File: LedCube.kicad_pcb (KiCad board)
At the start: 4 copper layers, 87.7 x 80.2 mm, 334 parts, among them CN1 B2B-XH-A (LF)(SN), CN2 B2B-XH-A (LF)(SN), J1 B10B-PHDSS-B_LF__SN_, J10 B10B-PHDSS-B_LF__SN_, J11 B10B-PHDSS-B_LF__SN_, J2 B10B-PHDSS-B_LF__SN_, J3 B10B-PHDSS-B_LF__SN_, J4 B10B-PHDSS-B_LF__SN_, J5 B10B-PHDSS-B_LF__SN_, J6 B10B-PHDSS-B_LF__SN_, J7 B10B-PHDSS-B_LF__SN_, J8 B10B-PHDSS-B_LF__SN_, J9 B10B-PHDSS-B_LF__SN_, Q1 AO3400A, Q10 AO3400A, Q11 JSM7409B, Q13 JSM7409B, Q2 AO3400A, Q3 AO3400A, Q4 AO3400A, Q5 AO3400A, Q6 AO3400A, Q7 AO3400A, Q8 AO3400A, Q9 AO3400A, SW2 TS-1088-AR02016, U1 STM32H743VGTx, U10 SN74LVC373ARGYR, U11 SN74LVC373ARGYR, U12 SN74LVC373ARGYR, U13 SN74LVC373ARGYR, U14 SN74LVC373ARGYR, U15 SN74LVC373ARGYR, U16 SN74LVC373ARGYR, U17 SN74LVC373ARGYR, U18 SN74LVC373ARGYR, U19 SN74LVC373ARGYR, U2 M95M04-DRMN6TP, U20 STUSB4500QTR, U21 ASM330LHBG1TR, U22 IIS2MDCTR, U23 TMP117xxDRV, U24 CC1101RGPR, U25 CC1101RGPR, U3 B3B-XH-A(LF)(SN), U4 B4B-XH-A(LF)(SN), U5 HC-PHD2.0-2X3A, U6 TPS56637RPAR, U7 SN74LVC373ARGYR, U8 SN74LVC373ARGYR, U9 SN74LVC373ARGYR, X1 Q13FC1350000400, Y1 MDH 2.D.1.480008813, Y3 Crystal_GND24, Y4 Crystal_GND24

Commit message: Update PCB layout
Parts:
- added REF**: MountingHole_2mm, MountingHole:MountingHole_2mm, F.Cu at (117.9, 38.6)
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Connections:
- D14 pad 4: unconnected-(D14-K3-Pad4) -> Net-(D14-K3)
- D14 pad 5: unconnected-(D14-K4-Pad5) -> Net-(D14-K4)
- D14 pad 8: Net-(D14-K7) -> unconnected-(D14-K7-Pad8)
- D14 pad 9: Net-(D14-K8) -> unconnected-(D14-K8-Pad9)
- D15 pad 4: unconnected-(D15-K3-Pad4) -> Net-(D15-K3)
- D15 pad 5: unconnected-(D15-K4-Pad5) -> Net-(D15-K4)
- D15 pad 6: Net-(D15-K5) -> unconnected-(D15-K5-Pad6)
- D15 pad 7: Net-(D15-K6) -> unconnected-(D15-K6-Pad7)
- D18 pad 4: Net-(D18-K3) -> unconnected-(D18-K3-Pad4)
- D18 pad 8: unconnected-(D18-K7-Pad8) -> Net-(D18-K7)
- D19 pad 2: Net-(D19-K2) -> unconnected-(D19-K2-Pad2)
- D19 pad 7: unconnected-(D19-K6-Pad7) -> Net-(D19-K6)
- D8 pad 2: Net-(D8-K2) -> unconnected-(D8-K2-Pad2)
- D8 pad 9: Net-(D8-K8) -> Net-(D5-K1)
- J1 pad 1: Net-(J1-Pad1) -> Net-(D5-K1)
- J1 pad 10: Net-(J1-Pad10) -> Net-(D5-K8)
- J1 pad 2: Net-(J1-Pad2) -> Net-(D8-K1)
- J1 pad 3: Net-(J1-Pad3) -> Net-(D5-K5)
- J1 pad 4: Net-(J1-Pad4) -> Net-(D5-K4)
- J1 pad 5: Net-(J1-Pad5) -> Net-(D5-K6)
- J1 pad 6: Net-(J1-Pad6) -> Net-(D5-K3)
- J1 pad 7: Net-(J1-Pad7) -> Net-(D5-K2)
- J1 pad 8: Net-(J1-Pad8) -> Net-(D5-K7)
- J1 pad 9: Net-(J1-Pad9) -> Net-(D5-K1)
- J10 pad 1: Net-(J10-Pad1) -> Net-(D16-K7)
- J10 pad 10: Net-(J10-Pad10) -> Net-(D17-K4)
- J10 pad 2: Net-(J10-Pad2) -> Net-(D17-K8)
- J10 pad 3: Net-(J10-Pad3) -> Net-(D16-K8)
- J10 pad 4: Net-(J10-Pad4) -> Net-(D17-K7)
- J10 pad 5: Net-(J10-Pad5) -> Net-(D17-K1)
- J10 pad 6: Net-(J10-Pad6) -> Net-(D17-K6)
- J10 pad 7: Net-(J10-Pad7) -> Net-(D17-K2)
- J10 pad 8: Net-(J10-Pad8) -> Net-(D17-K5)
- J10 pad 9: Net-(J10-Pad9) -> Net-(D17-K3)
- J11 pad 3: Net-(D19-K2) -> Net-(D19-K3)
- J11 pad 4: Net-(D19-K3) -> Net-(D19-K6)
- J11 pad 8: Net-(D18-K3) -> Net-(D18-K7)
- J2 pad 1: Net-(J2-Pad1) -> Net-(D6-K1)
- J2 pad 10: Net-(J2-Pad10) -> Net-(D6-K6)
- J2 pad 2: Net-(J2-Pad2) -> Net-(D9-K2)
- J2 pad 3: Net-(J2-Pad3) -> Net-(D6-K2)
- J2 pad 4: Net-(J2-Pad4) -> Net-(D9-K1)
- J2 pad 5: Net-(J2-Pad5) -> Net-(D6-K3)
- J2 pad 6: Net-(J2-Pad6) -> Net-(D6-K8)
- J2 pad 7: Net-(J2-Pad7) -> Net-(D6-K4)
- J2 pad 8: Net-(J2-Pad8) -> Net-(D6-K7)
- J2 pad 9: Net-(J2-Pad9) -> Net-(D6-K5)
- J3 pad 1: Net-(J3-Pad1) -> Net-(D7-K1)
- J3 pad 10: Net-(J3-Pad10) -> Net-(D7-K6)
- J3 pad 2: Net-(J3-Pad2) -> Net-(D10-K2)
- J3 pad 3: Net-(J3-Pad3) -> Net-(D7-K2)
- J3 pad 4: Net-(J3-Pad4) -> Net-(D10-K1)
- J3 pad 5: Net-(J3-Pad5) -> Net-(D7-K3)
- J3 pad 6: Net-(J3-Pad6) -> Net-(D7-K8)
- J3 pad 7: Net-(J3-Pad7) -> Net-(D7-K4)
- J3 pad 8: Net-(J3-Pad8) -> Net-(D7-K7)
- J3 pad 9: Net-(J3-Pad9) -> Net-(D7-K5)
- J4 pad 1: Net-(J4-Pad1) -> Net-(D8-K3)
- J4 pad 2: Net-(J4-Pad2) -> Net-(D11-K4)
- J4 pad 3: Net-(J4-Pad3) -> Net-(D8-K4)
- J4 pad 4: Net-(J4-Pad4) -> Net-(D11-K3)
- J4 pad 5: Net-(J4-Pad5) -> Net-(D8-K5)
- J4 pad 6: Net-(J4-Pad6) -> Net-(D11-K2)
- J4 pad 7: Net-(J4-Pad7) -> Net-(D8-K6)
- J4 pad 8: Net-(J4-Pad8) -> Net-(D11-K1)
- J4 pad 9: Net-(J4-Pad9) -> Net-(D8-K7)
- J5 pad 1: Net-(J5-Pad1) -> Net-(D9-K3)
- J5 pad 10: Net-(J5-Pad10) -> Net-(D9-K8)
- J5 pad 2: Net-(J5-Pad2) -> Net-(D12-K4)
- J5 pad 3: Net-(J5-Pad3) -> Net-(D9-K4)
- J5 pad 4: Net-(J5-Pad4) -> Net-(D12-K3)
- J5 pad 5: Net-(J5-Pad5) -> Net-(D9-K5)
- J5 pad 6: Net-(J5-Pad6) -> Net-(D12-K2)
- J5 pad 7: Net-(J5-Pad7) -> Net-(D9-K6)
- J5 pad 8: Net-(J5-Pad8) -> Net-(D12-K1)
- J5 pad 9: Net-(J5-Pad9) -> Net-(D9-K7)
- J6 pad 1: Net-(J6-Pad1) -> Net-(D10-K3)
- J6 pad 10: Net-(J6-Pad10) -> Net-(D10-K8)
- J6 pad 2: Net-(J6-Pad2) -> Net-(D13-K4)
- J6 pad 3: Net-(J6-Pad3) -> Net-(D10-K4)
- J6 pad 4: Net-(J6-Pad4) -> Net-(D13-K3)
- J6 pad 5: Net-(J6-Pad5) -> Net-(D10-K5)
- J6 pad 6: Net-(J6-Pad6) -> Net-(D13-K2)
- J6 pad 7: Net-(J6-Pad7) -> Net-(D10-K6)
- J6 pad 8: Net-(J6-Pad8) -> Net-(D13-K1)
- J6 pad 9: Net-(J6-Pad9) -> Net-(D10-K7)
- J7 pad 1: Net-(J7-Pad1) -> Net-(D11-K5)
- J7 pad 10: Net-(J7-Pad10) -> Net-(D14-K2)
- J7 pad 2: Net-(J7-Pad2) -> Net-(D14-K6)
- J7 pad 3: Net-(J7-Pad3) -> Net-(D11-K6)
- J7 pad 4: Net-(J7-Pad4) -> Net-(D14-K5)
- J7 pad 5: Net-(J7-Pad5) -> Net-(D11-K7)
- J7 pad 6: Net-(J7-Pad6) -> Net-(D14-K4)
- J7 pad 7: Net-(J7-Pad7) -> Net-(D11-K8)
- J7 pad 8: Net-(J7-Pad8) -> Net-(D14-K3)
- J7 pad 9: Net-(J7-Pad9) -> Net-(D14-K1)
- J8 pad 1: Net-(J8-Pad1) -> Net-(D12-K5)
- J8 pad 10: Net-(J8-Pad10) -> Net-(D15-K2)
- J8 pad 2: Net-(J8-Pad2) -> Net-(D15-K8)
- J8 pad 3: Net-(J8-Pad3) -> Net-(D12-K6)
- J8 pad 4: Net-(J8-Pad4) -> Net-(D15-K7)
- J8 pad 5: Net-(J8-Pad5) -> Net-(D12-K7)
- J8 pad 6: Net-(J8-Pad6) -> Net-(D15-K4)
- J8 pad 7: Net-(J8-Pad7) -> Net-(D12-K8)
- J8 pad 8: Net-(J8-Pad8) -> unconnected-(J8-Pad8)
- J8 pad 9: Net-(J8-Pad9) -> Net-(D15-K1)
- J9 pad 1: Net-(J9-Pad1) -> Net-(D13-K5)
- J9 pad 10: Net-(J9-Pad10) -> Net-(D16-K2)
- J9 pad 2: Net-(J9-Pad2) -> Net-(D16-K6)
- J9 pad 3: Net-(J9-Pad3) -> Net-(D13-K6)
- J9 pad 4: Net-(J9-Pad4) -> Net-(D16-K5)
- J9 pad 5: Net-(J9-Pad5) -> Net-(D13-K7)
- J9 pad 6: Net-(J9-Pad6) -> Net-(D16-K4)
- J9 pad 7: Net-(J9-Pad7) -> Net-(D13-K8)
- J9 pad 8: Net-(J9-Pad8) -> Net-(D16-K3)
- J9 pad 9: Net-(J9-Pad9) -> Net-(D16-K1)
- Q11 pad 6: /USB-PD/V_SINK -> (no net)
- Q11 pad 7: /USB-PD/V_SINK -> (no net)
- Q11 pad 8: /USB-PD/V_SINK -> (no net)
- Q13 pad 6: Net-(D21-K) -> (no net)
- Q13 pad 7: Net-(D21-K) -> (no net)
- Q13 pad 8: Net-(D21-K) -> (no net)
- Q2 pad 3: Net-(D18-K3) -> Net-(D18-K7)
- Q4 pad 3: Net-(D19-K3) -> Net-(D19-K6)
- Q7 pad 3: Net-(D19-K2) -> Net-(D19-K3)
- R100 pad 1: Net-(J9-Pad10) -> Net-(D16-K2)
- R100 pad 2: Net-(D16-K2) -> Net-(U18-2Q)
- R101 pad 1: Net-(J9-Pad8) -> Net-(D16-K3)
- R101 pad 2: Net-(D16-K8) -> Net-(U18-3Q)
- R102 pad 1: Net-(J9-Pad6) -> Net-(D16-K4)
- R102 pad 2: Net-(D16-K7) -> Net-(U18-4Q)
- R103 pad 1: Net-(J9-Pad4) -> unconnected-(R103-Pad1)
- R103 pad 2: Net-(D16-K6) -> Net-(D16-K5)
- R104 pad 1: Net-(J9-Pad2) -> unconnected-(R104-Pad1)
- R104 pad 2: Net-(D16-K5) -> Net-(D16-K6)
- R105 pad 1: Net-(D17-K8) -> Net-(D17-K3)
- R105 pad 2: Net-(J10-Pad9) -> Net-(U19-3Q)
- R106 pad 2: Net-(J10-Pad7) -> Net-(U19-2Q)
- R107 pad 2: Net-(J10-Pad5) -> Net-(U19-1Q)
- R108 pad 1: Net-(D16-K4) -> unconnected-(R108-Pad1)
- R108 pad 2: Net-(J10-Pad3) -> Net-(D16-K8)
- R109 pad 1: Net-(D16-K3) -> unconnected-(R109-Pad1)
- R109 pad 2: Net-(J10-Pad1) -> Net-(D16-K7)
- R110 pad 1: Net-(J10-Pad10) -> Net-(D17-K4)
- R110 pad 2: Net-(D17-K7) -> Net-(U19-4Q)
- R111 pad 1: Net-(J10-Pad8) -> unconnected-(R111-Pad1)
- R111 pad 2: Net-(D17-K6) -> Net-(D17-K5)
- R112 pad 1: Net-(J10-Pad6) -> unconnected-(R112-Pad1)
- R112 pad 2: Net-(D17-K5) -> Net-(D17-K6)
- R113 pad 1: Net-(J10-Pad4) -> unconnected-(R113-Pad1)
- R113 pad 2: Net-(D17-K3) -> Net-(D17-K7)
- R114 pad 1: Net-(J10-Pad2) -> unconnected-(R114-Pad1)
- R114 pad 2: Net-(D17-K4) -> Net-(D17-K8)
- R15 pad 1: Net-(D5-K6) -> Net-(D5-K5)
- R15 pad 2: Net-(J1-Pad9) -> unconnected-(R15-Pad2)
- R16 pad 1: Net-(D5-K7) -> unconnected-(R16-Pad1)
- R16 pad 2: Net-(J1-Pad7) -> Net-(D5-K4)
- R17 pad 1: Net-(D5-K8) -> unconnected-(R17-Pad1)
- R17 pad 2: Net-(J1-Pad5) -> Net-(D5-K3)
- R18 pad 1: Net-(D5-K2) -> Net-(U7-3Q)
- R18 pad 2: Net-(J1-Pad3) -> Net-(D5-K2)
- R19 pad 2: Net-(J1-Pad1) -> Net-(U7-1Q)
- R20 pad 1: Net-(D8-K3) -> unconnected-(R20-Pad1)
- R20 pad 2: Net-(J4-Pad9) -> Net-(D8-K7)
- R21 pad 1: Net-(D8-K5) -> unconnected-(R21-Pad1)
- R21 pad 2: Net-(J4-Pad7) -> Net-(D8-K6)
- R22 pad 1: Net-(D8-K6) -> unconnected-(R22-Pad1)
- R22 pad 2: Net-(J4-Pad5) -> Net-(D8-K5)
- R23 pad 1: Net-(D8-K7) -> Net-(D8-K4)
- R23 pad 2: Net-(J4-Pad3) -> Net-(U10-4Q)
- R24 pad 1: Net-(D8-K8) -> Net-(D8-K3)
- R24 pad 2: Net-(J4-Pad1) -> Net-(U10-3Q)
- R25 pad 1: Net-(J4-Pad10) -> unconnected-(R25-Pad1)
- R25 pad 2: Net-(D8-K4) -> Net-(J4-Pad10)
- R26 pad 1: Net-(J4-Pad8) -> Net-(D11-K1)
- R26 pad 2: Net-(D11-K1) -> Net-(U13-1Q)
- R27 pad 1: Net-(J4-Pad6) -> Net-(D11-K2)
- R27 pad 2: Net-(D11-K2) -> Net-(U13-2Q)
- R28 pad 1: Net-(J4-Pad4) -> Net-(D11-K3)
- R28 pad 2: Net-(D11-K8) -> Net-(U13-3Q)
- R29 pad 1: Net-(J4-Pad2) -> Net-(D11-K4)
- R29 pad 2: Net-(D11-K7) -> Net-(U13-4Q)
- R30 pad 1: Net-(J1-Pad10) -> Net-(D5-K6)
- R30 pad 2: Net-(D5-K5) -> unconnected-(R30-Pad2)
- R31 pad 1: Net-(J1-Pad8) -> Net-(D5-K6)
- R31 pad 2: Net-(D5-K3) -> Net-(U7-4Q)
- R32 pad 1: Net-(J1-Pad6) -> Net-(D5-K8)
- R32 pad 2: Net-(D5-K4) -> Net-(U7-2Q)
- R33 pad 1: Net-(J1-Pad4) -> Net-(D5-K4)
- R33 pad 2: Net-(D8-K1) -> Net-(U10-1Q)
- R34 pad 1: Net-(J1-Pad2) -> Net-(D8-K1)
- R34 pad 2: Net-(D8-K2) -> Net-(U10-2Q)
- R35 pad 2: Net-(J7-Pad9) -> Net-(U16-1Q)
- R36 pad 1: Net-(D11-K4) -> unconnected-(R36-Pad1)
- R36 pad 2: Net-(J7-Pad7) -> Net-(D11-K8)
- R37 pad 1: Net-(D11-K3) -> unconnected-(R37-Pad1)
- R37 pad 2: Net-(J7-Pad5) -> Net-(D11-K7)
- R38 pad 1: Net-(D11-K5) -> unconnected-(R38-Pad1)
- R38 pad 2: Net-(J7-Pad3) -> Net-(D11-K6)
- R39 pad 1: Net-(D11-K6) -> unconnected-(R39-Pad1)
- R39 pad 2: Net-(J7-Pad1) -> Net-(D11-K5)
- R40 pad 1: Net-(J7-Pad10) -> Net-(D14-K2)
- R40 pad 2: Net-(D14-K2) -> Net-(U16-2Q)
- R41 pad 1: Net-(J7-Pad8) -> Net-(D14-K3)
- R41 pad 2: Net-(D14-K8) -> Net-(U16-3Q)
- R42 pad 1: Net-(J7-Pad6) -> Net-(D14-K4)
- R42 pad 2: Net-(D14-K7) -> Net-(U16-4Q)
- R43 pad 1: Net-(J7-Pad4) -> unconnected-(R43-Pad1)
- R43 pad 2: Net-(D14-K6) -> Net-(D14-K5)
- R44 pad 1: Net-(J7-Pad2) -> unconnected-(R44-Pad1)
- R44 pad 2: Net-(D14-K5) -> Net-(D14-K6)
- R45 pad 1: Net-(D6-K6) -> unconnected-(R45-Pad1)
- R45 pad 2: Net-(J2-Pad9) -> Net-(D6-K5)
- R46 pad 1: Net-(D6-K7) -> Net-(D6-K4)
- R46 pad 2: Net-(J2-Pad7) -> Net-(U8-4Q)
- R47 pad 1: Net-(D6-K8) -> Net-(D6-K3)
- R47 pad 2: Net-(J2-Pad5) -> Net-(U8-3Q)
- R48 pad 2: Net-(J2-Pad3) -> Net-(U8-2Q)
- R49 pad 2: Net-(J2-Pad1) -> Net-(U8-1Q)
- R50 pad 1: Net-(J2-Pad10) -> unconnected-(R50-Pad1)
- R50 pad 2: Net-(D6-K5) -> Net-(D6-K6)
- R51 pad 1: Net-(J2-Pad8) -> unconnected-(R51-Pad1)
- R51 pad 2: Net-(D6-K3) -> Net-(D6-K7)
- R52 pad 1: Net-(J2-Pad6) -> unconnected-(R52-Pad1)
- R52 pad 2: Net-(D6-K4) -> Net-(D6-K8)
- R53 pad 1: Net-(J2-Pad4) -> Net-(D9-K1)
- R53 pad 2: Net-(D9-K1) -> Net-(U11-1Q)
- R54 pad 1: Net-(J2-Pad2) -> Net-(D9-K2)
- R54 pad 2: Net-(D9-K2) -> Net-(U11-2Q)
- R55 pad 1: Net-(D9-K3) -> unconnected-(R55-Pad1)
- R55 pad 2: Net-(J5-Pad9) -> Net-(D9-K7)
- R56 pad 1: Net-(D9-K5) -> unconnected-(R56-Pad1)
- R56 pad 2: Net-(J5-Pad7) -> Net-(D9-K6)
- R57 pad 1: Net-(D9-K6) -> unconnected-(R57-Pad1)
- R57 pad 2: Net-(J5-Pad5) -> Net-(D9-K5)
- R58 pad 1: Net-(D9-K7) -> Net-(D9-K4)
- R58 pad 2: Net-(J5-Pad3) -> Net-(U11-4Q)
- R59 pad 1: Net-(D9-K8) -> Net-(D9-K3)
- R59 pad 2: Net-(J5-Pad1) -> Net-(U11-3Q)
- R60 pad 1: Net-(J5-Pad10) -> unconnected-(R60-Pad1)
- R60 pad 2: Net-(D9-K4) -> Net-(D9-K8)
- R61 pad 1: Net-(J5-Pad8) -> Net-(D12-K1)
- R61 pad 2: Net-(D12-K1) -> Net-(U14-1Q)
- R62 pad 1: Net-(J5-Pad6) -> Net-(D12-K3)
- R62 pad 2: Net-(D12-K2) -> Net-(U14-3Q)
- R63 pad 1: Net-(J5-Pad4) -> Net-(D12-K6)
- R63 pad 2: Net-(D12-K8) -> unconnected-(R63-Pad2)
- R64 pad 1: Net-(J5-Pad2) -> Net-(D12-K8)
- R64 pad 2: Net-(D12-K7) -> unconnected-(R64-Pad2)
- R65 pad 2: Net-(J8-Pad9) -> Net-(U17-1Q)
- R66 pad 1: Net-(D12-K4) -> Net-(U14-4Q)
- R66 pad 2: Net-(J8-Pad7) -> Net-(D12-K4)
- R67 pad 1: Net-(D12-K3) -> Net-(D12-K2)
- R67 pad 2: Net-(J8-Pad5) -> Net-(U14-2Q)
- R68 pad 1: Net-(D12-K5) -> unconnected-(R68-Pad1)
- R68 pad 2: Net-(J8-Pad3) -> Net-(D12-K5)
- R69 pad 1: Net-(D12-K6) -> unconnected-(R69-Pad1)
- R69 pad 2: Net-(J8-Pad1) -> Net-(D12-K7)
- R70 pad 1: Net-(J8-Pad10) -> Net-(D15-K2)
- R70 pad 2: Net-(D15-K2) -> Net-(U17-3Q)
- R71 pad 1: Net-(J8-Pad8) -> Net-(D15-K3)
- R71 pad 2: Net-(D15-K8) -> unconnected-(R71-Pad2)
- R72 pad 1: Net-(J8-Pad6) -> Net-(D15-K4)
- R72 pad 2: Net-(D15-K7) -> unconnected-(R72-Pad2)
- R73 pad 1: Net-(J8-Pad4) -> Net-(U17-4Q)
- R73 pad 2: Net-(D15-K6) -> Net-(D15-K7)
- R74 pad 1: Net-(J8-Pad2) -> Net-(U17-2Q)
- R74 pad 2: Net-(D15-K5) -> Net-(D15-K8)
- R75 pad 1: Net-(D7-K6) -> unconnected-(R75-Pad1)
- R75 pad 2: Net-(J3-Pad9) -> Net-(D7-K5)
- R76 pad 1: Net-(D7-K7) -> Net-(D7-K4)
- R76 pad 2: Net-(J3-Pad7) -> Net-(U9-4Q)
- R77 pad 1: Net-(D7-K8) -> Net-(D7-K3)
- R77 pad 2: Net-(J3-Pad5) -> Net-(U9-3Q)
- R78 pad 2: Net-(J3-Pad3) -> Net-(U9-2Q)
- R79 pad 2: Net-(J3-Pad1) -> Net-(U9-1Q)
- R80 pad 1: Net-(J3-Pad10) -> unconnected-(R80-Pad1)
- R80 pad 2: Net-(D7-K5) -> Net-(D7-K6)
- R81 pad 1: Net-(J3-Pad8) -> unconnected-(R81-Pad1)
- R81 pad 2: Net-(D7-K3) -> Net-(D7-K7)
- R82 pad 1: Net-(J3-Pad6) -> unconnected-(R82-Pad1)
- R82 pad 2: Net-(D7-K4) -> Net-(D7-K8)
- R83 pad 1: Net-(J3-Pad4) -> Net-(D10-K1)
- R83 pad 2: Net-(D10-K1) -> Net-(U12-1Q)
- R84 pad 1: Net-(J3-Pad2) -> Net-(D10-K2)
- R84 pad 2: Net-(D10-K2) -> Net-(U12-2Q)
- R85 pad 1: Net-(D10-K3) -> unconnected-(R85-Pad1)
- R85 pad 2: Net-(J6-Pad9) -> Net-(D10-K7)
- R86 pad 1: Net-(D10-K5) -> unconnected-(R86-Pad1)
- R86 pad 2: Net-(J6-Pad7) -> Net-(D10-K6)
- R87 pad 1: Net-(D10-K6) -> unconnected-(R87-Pad1)
- R87 pad 2: Net-(J6-Pad5) -> Net-(D10-K5)
- R88 pad 1: Net-(D10-K7) -> Net-(D10-K4)
- R88 pad 2: Net-(J6-Pad3) -> Net-(U12-4Q)
- R89 pad 1: Net-(D10-K8) -> Net-(D10-K3)
- R89 pad 2: Net-(J6-Pad1) -> Net-(U12-3Q)
- R90 pad 1: Net-(J6-Pad10) -> unconnected-(R90-Pad1)
- R90 pad 2: Net-(D10-K4) -> Net-(D10-K8)
- R91 pad 1: Net-(J6-Pad8) -> Net-(D13-K1)
- R91 pad 2: Net-(D13-K1) -> Net-(U15-1Q)
- R92 pad 1: Net-(J6-Pad6) -> Net-(D13-K2)
- R92 pad 2: Net-(D13-K2) -> Net-(U15-2Q)
- R93 pad 1: Net-(J6-Pad4) -> Net-(D13-K3)
- R93 pad 2: Net-(D13-K8) -> Net-(U15-3Q)
- R94 pad 1: Net-(J6-Pad2) -> Net-(D13-K4)
- R94 pad 2: Net-(D13-K7) -> Net-(U15-4Q)
- R95 pad 2: Net-(J9-Pad9) -> Net-(U18-1Q)
- R96 pad 1: Net-(D13-K4) -> unconnected-(R96-Pad1)
- R96 pad 2: Net-(J9-Pad7) -> Net-(D13-K8)
- R97 pad 1: Net-(D13-K3) -> unconnected-(R97-Pad1)
- R97 pad 2: Net-(J9-Pad5) -> Net-(D13-K7)
- R98 pad 1: Net-(D13-K5) -> unconnected-(R98-Pad1)
- R98 pad 2: Net-(J9-Pad3) -> Net-(D13-K6)
- R99 pad 1: Net-(D13-K6) -> unconnected-(R99-Pad1)
- R99 pad 2: Net-(J9-Pad1) -> Net-(D13-K5)
- U10 pad 11: /Core/LE1 -> unconnected-(U10-LE-Pad11)
- U10 pad 12: Net-(D8-K6) -> unconnected-(U10-5Q-Pad12)
- U10 pad 13: /Core/D5 -> unconnected-(U10-5D-Pad13)
- U10 pad 14: /Core/D6 -> unconnected-(U10-6D-Pad14)
- U10 pad 15: Net-(D8-K5) -> unconnected-(U10-6Q-Pad15)
- U10 pad 16: Net-(D8-K3) -> unconnected-(U10-7Q-Pad16)
- U10 pad 17: /Core/D7 -> unconnected-(U10-7D-Pad17)
- U10 pad 18: /Core/D8 -> unconnected-(U10-8D-Pad18)
- U10 pad 19: Net-(D8-K4) -> unconnected-(U10-8Q-Pad19)
- U10 pad 2: Net-(D8-K1) -> Net-(U10-1Q)
- U10 pad 20: +3.3V -> unconnected-(U10-VCC-Pad20)
- U10 pad 21: GND -> unconnected-(U10-EPAD-Pad21)
- U10 pad 5: Net-(D8-K2) -> Net-(U10-2Q)
- U10 pad 6: Net-(D8-K8) -> Net-(U10-3Q)
- U10 pad 9: Net-(D8-K7) -> Net-(U10-4Q)
- U10 pad V: GND -> (no net)
- U11 pad 11: /Core/LE5 -> unconnected-(U11-LE-Pad11)
- U11 pad 12: Net-(D9-K6) -> unconnected-(U11-5Q-Pad12)
- U11 pad 13: /Core/D5 -> unconnected-(U11-5D-Pad13)
- U11 pad 14: /Core/D6 -> unconnected-(U11-6D-Pad14)
- U11 pad 15: Net-(D9-K5) -> unconnected-(U11-6Q-Pad15)
- U11 pad 16: Net-(D9-K3) -> unconnected-(U11-7Q-Pad16)
- U11 pad 17: /Core/D7 -> unconnected-(U11-7D-Pad17)
- U11 pad 18: /Core/D8 -> unconnected-(U11-8D-Pad18)
- U11 pad 19: Net-(D9-K4) -> unconnected-(U11-8Q-Pad19)
- U11 pad 2: Net-(D9-K1) -> Net-(U11-1Q)
- U11 pad 20: +3.3V -> unconnected-(U11-VCC-Pad20)
- U11 pad 21: GND -> unconnected-(U11-EPAD-Pad21)
- U11 pad 5: Net-(D9-K2) -> Net-(U11-2Q)
- U11 pad 6: Net-(D9-K8) -> Net-(U11-3Q)
- U11 pad 9: Net-(D9-K7) -> Net-(U11-4Q)
- U11 pad V: GND -> (no net)
- U12 pad 11: /Core/LE9 -> unconnected-(U12-LE-Pad11)
- U12 pad 12: Net-(D10-K6) -> unconnected-(U12-5Q-Pad12)
- U12 pad 13: /Core/D5 -> unconnected-(U12-5D-Pad13)
- U12 pad 14: /Core/D6 -> unconnected-(U12-6D-Pad14)
- U12 pad 15: Net-(D10-K5) -> unconnected-(U12-6Q-Pad15)
- U12 pad 16: Net-(D10-K3) -> unconnected-(U12-7Q-Pad16)
- U12 pad 17: /Core/D7 -> unconnected-(U12-7D-Pad17)
- U12 pad 18: /Core/D8 -> unconnected-(U12-8D-Pad18)
- U12 pad 19: Net-(D10-K4) -> unconnected-(U12-8Q-Pad19)
- U12 pad 2: Net-(D10-K1) -> Net-(U12-1Q)
- U12 pad 20: +3.3V -> unconnected-(U12-VCC-Pad20)
- U12 pad 21: GND -> unconnected-(U12-EPAD-Pad21)
- U12 pad 5: Net-(D10-K2) -> Net-(U12-2Q)
- U12 pad 6: Net-(D10-K8) -> Net-(U12-3Q)
- U12 pad 9: Net-(D10-K7) -> Net-(U12-4Q)
- U12 pad V: GND -> (no net)
- U13 pad 11: /Core/LE2 -> unconnected-(U13-LE-Pad11)
- U13 pad 12: Net-(D11-K6) -> unconnected-(U13-5Q-Pad12)
- U13 pad 13: /Core/D5 -> unconnected-(U13-5D-Pad13)
- U13 pad 14: /Core/D6 -> unconnected-(U13-6D-Pad14)
- U13 pad 15: Net-(D11-K5) -> unconnected-(U13-6Q-Pad15)
- U13 pad 16: Net-(D11-K3) -> unconnected-(U13-7Q-Pad16)
- U13 pad 17: /Core/D7 -> unconnected-(U13-7D-Pad17)
- U13 pad 18: /Core/D8 -> unconnected-(U13-8D-Pad18)
- U13 pad 19: Net-(D11-K4) -> unconnected-(U13-8Q-Pad19)
- U13 pad 2: Net-(D11-K1) -> Net-(U13-1Q)
- U13 pad 20: +3.3V -> unconnected-(U13-VCC-Pad20)
- U13 pad 21: GND -> unconnected-(U13-EPAD-Pad21)
- U13 pad 5: Net-(D11-K2) -> Net-(U13-2Q)
- U13 pad 6: Net-(D11-K8) -> Net-(U13-3Q)
- U13 pad 9: Net-(D11-K7) -> Net-(U13-4Q)
- U13 pad V: GND -> (no net)
- U14 pad 11: /Core/LE6 -> unconnected-(U14-LE-Pad11)
- U14 pad 12: Net-(D12-K6) -> unconnected-(U14-5Q-Pad12)
- U14 pad 13: /Core/D5 -> unconnected-(U14-5D-Pad13)
- U14 pad 14: /Core/D6 -> unconnected-(U14-6D-Pad14)
- U14 pad 15: Net-(D12-K5) -> unconnected-(U14-6Q-Pad15)
- U14 pad 16: Net-(D12-K3) -> unconnected-(U14-7Q-Pad16)
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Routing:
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
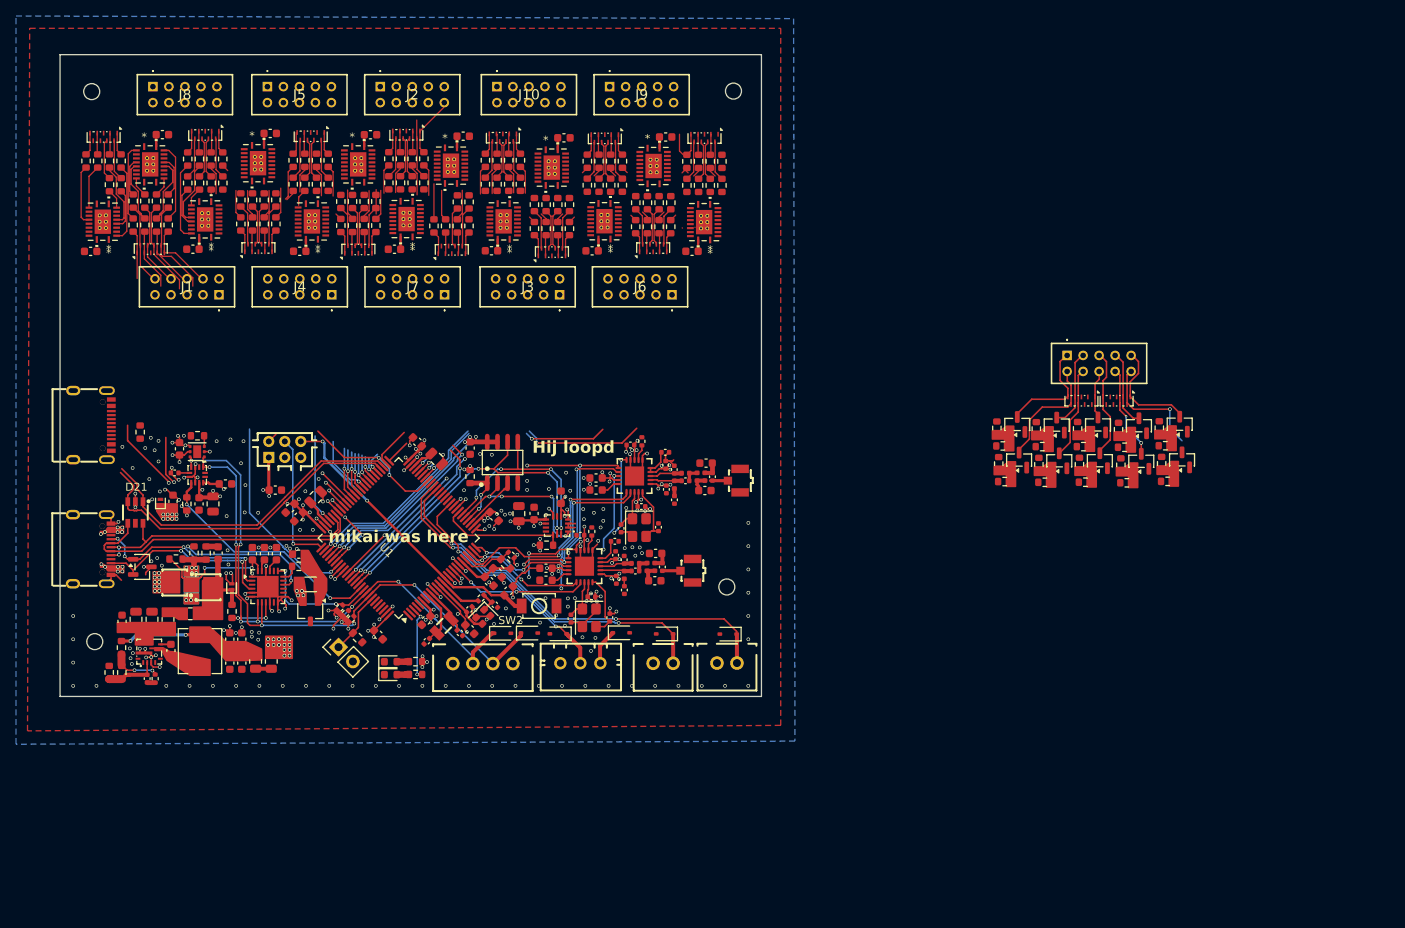
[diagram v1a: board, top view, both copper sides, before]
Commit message: Updated multiplexer routing
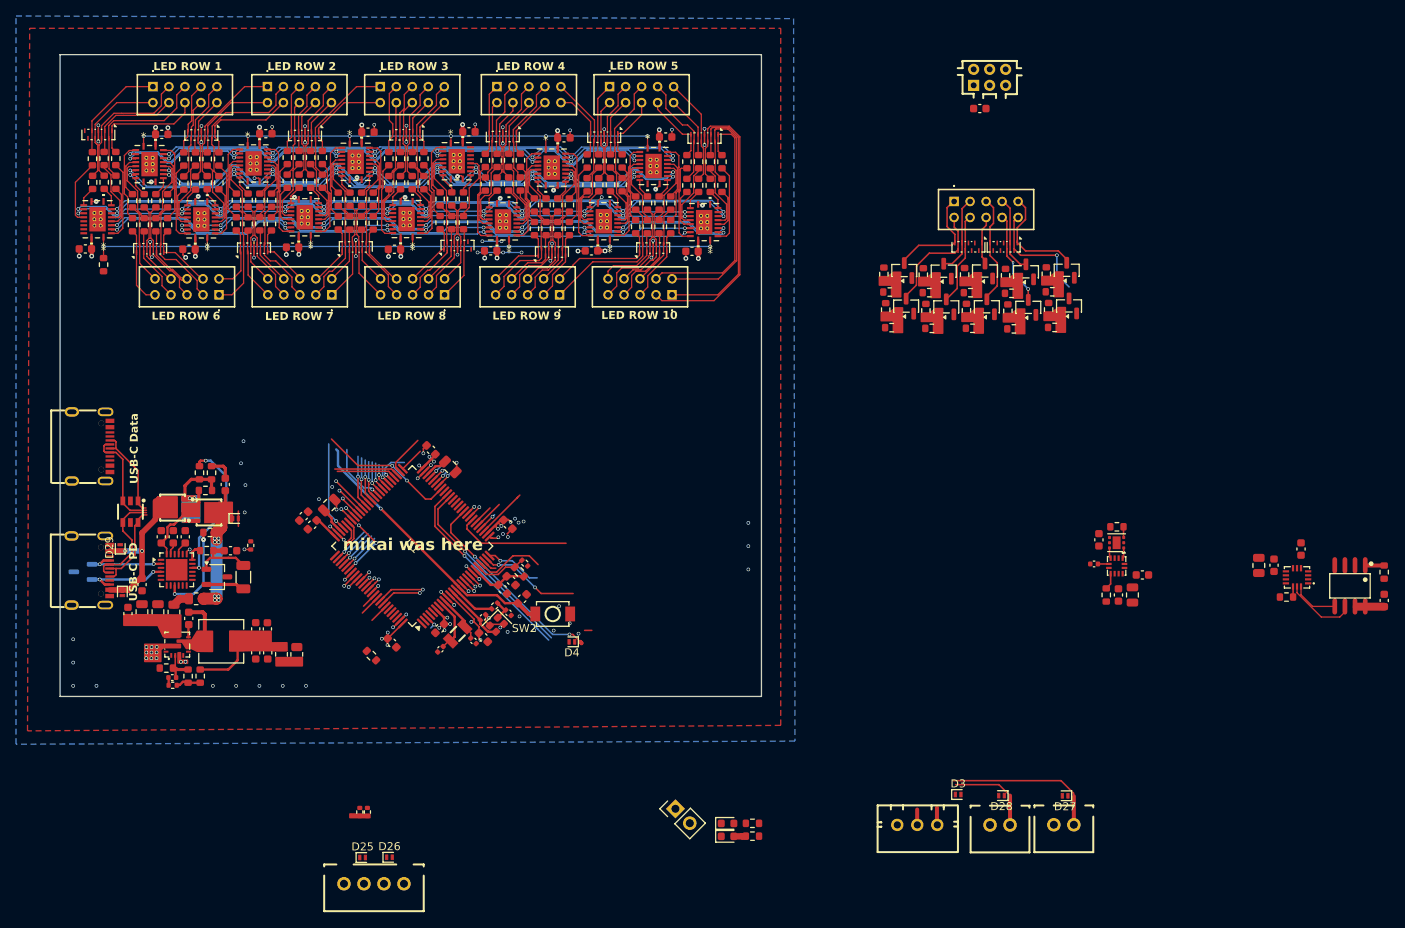
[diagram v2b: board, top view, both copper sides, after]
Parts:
- removed C56, C57, C58, C59: 100nF, Capacitor_SMD:C_0603_1608Metric
- removed C60, C61: 12pF, Capacitor_SMD:C_0402_1005Metric
- removed C62, C63, C68, C70, C72, C73, C75, C78, C83, C85: 220pF, Capacitor_SMD:C_0402_1005Metric
- removed C64, C65: 15pF, Capacitor_SMD:C_0402_1005Metric
- removed C66, C67, C69, C71: 10nF, Capacitor_SMD:C_0402_1005Metric
- removed C74, C76, C77, C79: 3.9pF, Capacitor_SMD:C_0402_1005Metric
- removed C80, C81: 8.2pF, Capacitor_SMD:C_0603_1608Metric
- removed C82, C84: 5.6pF, Capacitor_SMD:C_0603_1608Metric
- removed JP4, JP5: U.FL-R-SMT-1(80), easyeda2kicad:RF-SMD_FRF05002-JSS103M
- removed L2, L3, L4, L5, L8, L9: 27nH, Inductor_SMD:L_0402_1005Metric
- removed L6, L7: 22nH, Inductor_SMD:L_0402_1005Metric
- removed R144, R145: 56K, Resistor_SMD:R_0402_1005Metric
- removed REF** (x4): MountingHole_2mm, MountingHole:MountingHole_2mm
- removed U24, U25: CC1101RGPR, easyeda2kicad:QFN-20_L4.0-W4.0-P0.5-TL-EP
- removed Y3, Y4: Crystal_GND24, Crystal:Crystal_SMD_3225-4Pin_3.2x2.5mm
- added D29: ESDA25P35-1U1M, Diode_SMD:D_SOD-882, F.Cu at (41.2, 95.6)
- D22: moved to B.Cu
- D25, D26, D27, D28, D3, D4: footprint Diode_SMD:D_SOD-323 -> Diode_SMD:D_SOD-882
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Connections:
- D14 pad 5: Net-(D14-K4) -> unconnected-(D14-K4-Pad5)
- D14 pad 6: Net-(D14-K5) -> unconnected-(D14-K5-Pad6)
- D14 pad 8: unconnected-(D14-K7-Pad8) -> Net-(D14-K7)
- D14 pad 9: unconnected-(D14-K8-Pad9) -> Net-(D14-K8)
- D15 pad 5: Net-(D15-K4) -> unconnected-(D15-K4-Pad5)
- D15 pad 7: unconnected-(D15-K6-Pad7) -> Net-(D15-K6)
- D6 pad 1: Net-(D6-K1) -> /Multiplexer/Net-(D9-K1)
- D6 pad 4: Net-(D6-K3) -> /Multiplexer/Net-(D6-K1)
- D6 pad 7: Net-(D6-K6) -> /Multiplexer/Net-(D6-K8)
- D6 pad 8: Net-(D6-K7) -> /Multiplexer/Net-(D6-K7)
- D6 pad 9: Net-(D6-K8) -> /Multiplexer/Net-(D6-K4)
- D8 pad 2: unconnected-(D8-K2-Pad2) -> Net-(D8-K2)
- D8 pad 9: Net-(D5-K1) -> Net-(D8-K8)
- D9 pad 5: Net-(D9-K4) -> /Multiplexer/Net-(D9-K2)
- D9 pad 9: Net-(D9-K8) -> /Multiplexer/Net-(D9-K8)
- J1 pad 1: Net-(D5-K1) -> Net-(D8-K8)
- J10 pad 1: Net-(D16-K7) -> Net-(D17-K4)
- J10 pad 10: Net-(D17-K4) -> Net-(D16-K4)
- J10 pad 2: Net-(D17-K8) -> Net-(D17-K5)
- J10 pad 3: Net-(D16-K8) -> Net-(D17-K3)
- J10 pad 4: Net-(D17-K7) -> Net-(D17-K6)
- J10 pad 5: Net-(D17-K1) -> Net-(D17-K7)
- J10 pad 6: Net-(D17-K6) -> Net-(D17-K2)
- J10 pad 7: Net-(D17-K2) -> Net-(D17-K8)
- J10 pad 8: Net-(D17-K5) -> Net-(D17-K1)
- J10 pad 9: Net-(D17-K3) -> Net-(D16-K5)
- J2 pad 1: Net-(D6-K1) -> /Multiplexer/Net-(D9-K8)
- J2 pad 10: Net-(D6-K6) -> /Multiplexer/Net-(D9-K1)
- J2 pad 2: Net-(D9-K2) -> Net-(D9-K1)
- J2 pad 3: Net-(D6-K2) -> Net-(D6-K4)
- J2 pad 4: Net-(D9-K1) -> Net-(D6-K5)
- J2 pad 5: Net-(D6-K3) -> /Multiplexer/Net-(D6-K1)
- J2 pad 6: Net-(D6-K8) -> /Multiplexer/Net-(D6-K8)
- J2 pad 7: Net-(D6-K4) -> /Multiplexer/Net-(D6-K7)
- J2 pad 8: Net-(D6-K7) -> Net-(D6-K2)
- J2 pad 9: Net-(D6-K5) -> /Multiplexer/Net-(D6-K4)
- J3 pad 1: Net-(D7-K1) -> Net-(D10-K8)
- J3 pad 10: Net-(D7-K6) -> Net-(D7-K1)
- J3 pad 2: Net-(D10-K2) -> Net-(D10-K1)
- J3 pad 3: Net-(D7-K2) -> Net-(D7-K4)
- J3 pad 4: Net-(D10-K1) -> Net-(D7-K5)
- J3 pad 6: Net-(D7-K8) -> Net-(D7-K6)
- J3 pad 7: Net-(D7-K4) -> Net-(D7-K7)
- J3 pad 8: Net-(D7-K7) -> Net-(D7-K2)
- J3 pad 9: Net-(D7-K5) -> Net-(D7-K8)
- J4 pad 1: Net-(D8-K3) -> Net-(D11-K7)
- J4 pad 10: Net-(J4-Pad10) -> Net-(D8-K7)
- J4 pad 2: Net-(D11-K4) -> Net-(D11-K2)
- J4 pad 3: Net-(D8-K4) -> Net-(D11-K8)
- J4 pad 4: Net-(D11-K3) -> Net-(D11-K1)
- J4 pad 6: Net-(D11-K2) -> Net-(D8-K4)
- J4 pad 8: Net-(D11-K1) -> Net-(D8-K3)
- J4 pad 9: Net-(D8-K7) -> Net-(D8-K2)
- J5 pad 1: Net-(D9-K3) -> Net-(D12-K7)
- J5 pad 10: Net-(D9-K8) -> Net-(D9-K2)
- J5 pad 2: Net-(D12-K4) -> Net-(D12-K2)
- J5 pad 3: Net-(D9-K4) -> Net-(D12-K8)
- J5 pad 4: Net-(D12-K3) -> Net-(D12-K1)
- J5 pad 5: Net-(D9-K5) -> /Multiplexer/Net-(D9-K2)
- J5 pad 6: Net-(D12-K2) -> Net-(D9-K5)
- J5 pad 7: Net-(D9-K6) -> Net-(D9-K3)
- J5 pad 8: Net-(D12-K1) -> Net-(D9-K6)
- J6 pad 1: Net-(D10-K3) -> Net-(D13-K2)
- J6 pad 10: Net-(D10-K8) -> Net-(D10-K2)
- J6 pad 2: Net-(D13-K4) -> Net-(D13-K8)
- J6 pad 3: Net-(D10-K4) -> Net-(D13-K7)
- J6 pad 4: Net-(D13-K3) -> Net-(D13-K1)
- J6 pad 5: Net-(D10-K5) -> Net-(D10-K4)
- J6 pad 6: Net-(D13-K2) -> Net-(D10-K5)
- J6 pad 7: Net-(D10-K6) -> Net-(D10-K3)
- J6 pad 8: Net-(D13-K1) -> Net-(D10-K6)
- J7 pad 1: Net-(D11-K5) -> Net-(D14-K3)
- J7 pad 10: Net-(D14-K2) -> Net-(D11-K3)
- J7 pad 3: Net-(D11-K6) -> Net-(D14-K7)
- J7 pad 4: Net-(D14-K5) -> Net-(D14-K2)
- J7 pad 5: Net-(D11-K7) -> Net-(D14-K8)
- J7 pad 6: Net-(D14-K4) -> Net-(D14-K1)
- J7 pad 7: Net-(D11-K8) -> Net-(D11-K5)
- J7 pad 8: Net-(D14-K3) -> Net-(D11-K4)
- J7 pad 9: Net-(D14-K1) -> Net-(D11-K6)
- J8 pad 1: Net-(D12-K5) -> Net-(D15-K3)
- J8 pad 10: Net-(D15-K2) -> Net-(D12-K6)
- J8 pad 2: Net-(D15-K8) -> Net-(D15-K6)
- J8 pad 3: Net-(D12-K6) -> Net-(D15-K7)
- J8 pad 4: Net-(D15-K7) -> Net-(D15-K2)
- J8 pad 5: Net-(D12-K7) -> Net-(D15-K8)
- J8 pad 6: Net-(D15-K4) -> Net-(D15-K1)
- J8 pad 7: Net-(D12-K8) -> Net-(D12-K4)
- J8 pad 8: unconnected-(J8-Pad8) -> Net-(D12-K5)
- J8 pad 9: Net-(D15-K1) -> Net-(D12-K3)
- J9 pad 1: Net-(D13-K5) -> Net-(D16-K3)
- J9 pad 10: Net-(D16-K2) -> Net-(D13-K3)
- J9 pad 3: Net-(D13-K6) -> Net-(D16-K7)
- J9 pad 4: Net-(D16-K5) -> Net-(D16-K2)
- J9 pad 5: Net-(D13-K7) -> Net-(D16-K8)
- J9 pad 6: Net-(D16-K4) -> Net-(D16-K1)
- J9 pad 7: Net-(D13-K8) -> Net-(D13-K5)
- J9 pad 8: Net-(D16-K3) -> Net-(D13-K4)
- J9 pad 9: Net-(D16-K1) -> Net-(D13-K6)
- R100 pad 1: Net-(D16-K2) -> Net-(D16-K8)
- R101 pad 1: Net-(D16-K3) -> Net-(D16-K2)
- R102 pad 1: Net-(D16-K4) -> Net-(D16-K7)
- R103 pad 1: unconnected-(R103-Pad1) -> Net-(U18-5Q)
- R103 pad 2: Net-(D16-K5) -> Net-(D16-K6)
- R104 pad 1: unconnected-(R104-Pad1) -> Net-(U18-6Q)
- R104 pad 2: Net-(D16-K6) -> Net-(D16-K3)
- R105 pad 1: Net-(D17-K3) -> Net-(D17-K2)
- R106 pad 1: Net-(D17-K2) -> Net-(D17-K8)
- R108 pad 1: unconnected-(R108-Pad1) -> Net-(U18-8Q)
- R108 pad 2: Net-(D16-K8) -> Net-(D16-K4)
- R109 pad 1: unconnected-(R109-Pad1) -> Net-(U18-7Q)
- R109 pad 2: Net-(D16-K7) -> Net-(D16-K5)
- R110 pad 1: Net-(D17-K4) -> Net-(D17-K7)
- R111 pad 1: unconnected-(R111-Pad1) -> Net-(U19-5Q)
- R111 pad 2: Net-(D17-K5) -> Net-(D17-K6)
- R112 pad 1: unconnected-(R112-Pad1) -> Net-(U19-6Q)
- R112 pad 2: Net-(D17-K6) -> Net-(D17-K3)
- R113 pad 1: unconnected-(R113-Pad1) -> Net-(U19-7Q)
- R113 pad 2: Net-(D17-K7) -> Net-(D17-K5)
- R114 pad 1: unconnected-(R114-Pad1) -> Net-(U19-8Q)
- R114 pad 2: Net-(D17-K8) -> Net-(D17-K4)
- R15 pad 2: unconnected-(R15-Pad2) -> Net-(U7-7Q)
- R16 pad 1: unconnected-(R16-Pad1) -> Net-(U7-8Q)
- R17 pad 1: unconnected-(R17-Pad1) -> Net-(U7-6Q)
- R20 pad 1: unconnected-(R20-Pad1) -> Net-(D8-K5)
- R20 pad 2: Net-(D8-K7) -> Net-(U10-7Q)
- R21 pad 1: unconnected-(R21-Pad1) -> Net-(U10-6Q)
- R21 pad 2: Net-(D8-K6) -> Net-(D8-K3)
- R22 pad 1: unconnected-(R22-Pad1) -> Net-(U10-5Q)
- R22 pad 2: Net-(D8-K5) -> Net-(D8-K6)
- R23 pad 1: Net-(D8-K4) -> Net-(D8-K7)
- R24 pad 1: Net-(D8-K3) -> Net-(U10-3Q)
- R24 pad 2: Net-(U10-3Q) -> Net-(D8-K2)
- R25 pad 1: unconnected-(R25-Pad1) -> Net-(U10-8Q)
- R25 pad 2: Net-(J4-Pad10) -> Net-(D8-K4)
- R27 pad 1: Net-(D11-K2) -> Net-(D11-K8)
- R28 pad 1: Net-(D11-K3) -> Net-(D11-K2)
- R29 pad 1: Net-(D11-K4) -> Net-(D11-K7)
- R30 pad 2: unconnected-(R30-Pad2) -> Net-(U7-5Q)
- R31 pad 1: Net-(D5-K6) -> Net-(D5-K7)
- R33 pad 1: Net-(D5-K4) -> Net-(D8-K1)
- R34 pad 1: Net-(D8-K1) -> Net-(D8-K8)
- R36 pad 1: unconnected-(R36-Pad1) -> Net-(U13-8Q)
- R36 pad 2: Net-(D11-K8) -> Net-(D11-K4)
- R37 pad 1: unconnected-(R37-Pad1) -> Net-(U13-7Q)
- R37 pad 2: Net-(D11-K7) -> Net-(D11-K5)
- R38 pad 1: unconnected-(R38-Pad1) -> Net-(U13-6Q)
- R38 pad 2: Net-(D11-K6) -> Net-(D11-K3)
- R39 pad 1: unconnected-(R39-Pad1) -> Net-(U13-5Q)
- R39 pad 2: Net-(D11-K5) -> Net-(D11-K6)
- R40 pad 1: Net-(D14-K2) -> Net-(D14-K8)
- R41 pad 1: Net-(D14-K3) -> Net-(D14-K2)
- R42 pad 1: Net-(D14-K4) -> Net-(D14-K7)
- R43 pad 1: unconnected-(R43-Pad1) -> Net-(U16-5Q)
- R43 pad 2: Net-(D14-K5) -> Net-(D14-K6)
- R44 pad 1: unconnected-(R44-Pad1) -> Net-(U16-6Q)
- R44 pad 2: Net-(D14-K6) -> Net-(D14-K3)
- R45 pad 1: unconnected-(R45-Pad1) -> Net-(U8-5Q)
- R45 pad 2: Net-(D6-K5) -> /Multiplexer/Net-(D6-K8)
- R46 pad 1: Net-(D6-K4) -> /Multiplexer/Net-(D6-K7)
- R47 pad 1: Net-(D6-K3) -> Net-(D6-K2)
- R48 pad 1: Net-(D6-K2) -> /Multiplexer/Net-(D6-K4)
- R49 pad 1: Net-(D6-K1) -> /Multiplexer/Net-(D9-K1)
- R50 pad 1: unconnected-(R50-Pad1) -> Net-(U8-6Q)
- R50 pad 2: Net-(D6-K6) -> /Multiplexer/Net-(D6-K1)
- R51 pad 1: unconnected-(R51-Pad1) -> Net-(U8-7Q)
- R51 pad 2: Net-(D6-K7) -> Net-(D6-K5)
- R52 pad 1: unconnected-(R52-Pad1) -> Net-(U8-8Q)
- R52 pad 2: Net-(D6-K8) -> Net-(D6-K4)
- R54 pad 1: Net-(D9-K2) -> /Multiplexer/Net-(D9-K8)
- R55 pad 1: unconnected-(R55-Pad1) -> Net-(U11-7Q)
- R55 pad 2: Net-(D9-K7) -> Net-(D9-K5)
- R56 pad 1: unconnected-(R56-Pad1) -> Net-(U11-6Q)
- R56 pad 2: Net-(D9-K6) -> Net-(D9-K3)
- R57 pad 1: unconnected-(R57-Pad1) -> Net-(U11-5Q)
- R57 pad 2: Net-(D9-K5) -> Net-(D9-K6)
- R58 pad 1: Net-(D9-K4) -> Net-(D9-K7)
- R59 pad 1: Net-(D9-K3) -> Net-(D9-K2)
- R60 pad 1: unconnected-(R60-Pad1) -> Net-(U11-8Q)
- R60 pad 2: Net-(D9-K8) -> /Multiplexer/Net-(D9-K2)
- R62 pad 1: Net-(D12-K3) -> Net-(D12-K2)
- R63 pad 1: Net-(D12-K6) -> Net-(D12-K3)
- R63 pad 2: unconnected-(R63-Pad2) -> Net-(U14-6Q)
- R64 pad 1: Net-(D12-K8) -> Net-(D12-K7)
- R64 pad 2: unconnected-(R64-Pad2) -> Net-(U14-4Q)
- R66 pad 1: Net-(U14-4Q) -> Net-(U14-8Q)
- R67 pad 1: Net-(D12-K2) -> Net-(D12-K8)
- R68 pad 1: unconnected-(R68-Pad1) -> Net-(U14-5Q)
- R68 pad 2: Net-(D12-K5) -> Net-(D12-K6)
- R69 pad 1: unconnected-(R69-Pad1) -> Net-(U14-7Q)
- R69 pad 2: Net-(D12-K7) -> Net-(D12-K5)
- R71 pad 1: Net-(D15-K3) -> Net-(D15-K6)
- R71 pad 2: unconnected-(R71-Pad2) -> Net-(U17-5Q)
- R72 pad 1: Net-(D15-K4) -> Net-(D15-K3)
- R72 pad 2: unconnected-(R72-Pad2) -> Net-(U17-6Q)
- R75 pad 1: unconnected-(R75-Pad1) -> Net-(U9-5Q)
- R75 pad 2: Net-(D7-K5) -> Net-(D7-K6)
- R76 pad 1: Net-(D7-K4) -> Net-(D7-K7)
- R77 pad 1: Net-(D7-K3) -> Net-(D7-K2)
- R78 pad 1: Net-(D7-K2) -> Net-(D7-K8)
- R80 pad 1: unconnected-(R80-Pad1) -> Net-(U9-6Q)
- R80 pad 2: Net-(D7-K6) -> Net-(D7-K3)
- R81 pad 1: unconnected-(R81-Pad1) -> Net-(U9-7Q)
- R81 pad 2: Net-(D7-K7) -> Net-(D7-K5)
- R82 pad 1: unconnected-(R82-Pad1) -> Net-(U9-8Q)
- R82 pad 2: Net-(D7-K8) -> Net-(D7-K4)
- R84 pad 1: Net-(D10-K2) -> Net-(D10-K8)
- R85 pad 1: unconnected-(R85-Pad1) -> Net-(U12-7Q)
- R85 pad 2: Net-(D10-K7) -> Net-(D10-K5)
- R86 pad 1: unconnected-(R86-Pad1) -> Net-(U12-6Q)
- R86 pad 2: Net-(D10-K6) -> Net-(D10-K3)
- R87 pad 1: unconnected-(R87-Pad1) -> Net-(U12-5Q)
- R87 pad 2: Net-(D10-K5) -> Net-(D10-K6)
- R88 pad 1: Net-(D10-K4) -> Net-(D10-K7)
- R89 pad 1: Net-(D10-K3) -> Net-(D10-K2)
- R90 pad 1: unconnected-(R90-Pad1) -> Net-(U12-8Q)
- R90 pad 2: Net-(D10-K8) -> Net-(D10-K4)
- R92 pad 1: Net-(D13-K2) -> Net-(D13-K8)
- R93 pad 1: Net-(D13-K3) -> Net-(D13-K2)
- R94 pad 1: Net-(D13-K4) -> Net-(D13-K7)
- R96 pad 1: unconnected-(R96-Pad1) -> Net-(U15-8Q)
- R96 pad 2: Net-(D13-K8) -> Net-(D13-K4)
- R97 pad 1: unconnected-(R97-Pad1) -> Net-(U15-7Q)
- R97 pad 2: Net-(D13-K7) -> Net-(D13-K5)
- R98 pad 1: unconnected-(R98-Pad1) -> Net-(U15-6Q)
- R98 pad 2: Net-(D13-K6) -> Net-(D13-K3)
- R99 pad 1: unconnected-(R99-Pad1) -> Net-(U15-5Q)
- R99 pad 2: Net-(D13-K5) -> Net-(D13-K6)
- U1 pad 15: /BLE/BLE_SPI_CS1 -> /Core/BLE_SPI_CS_1
- U1 pad 16: /BLE/BLE_SPI_MOSI -> /Core/SPI2_MOSI
- U1 pad 17: /BLE/BLE_SPI_MISO -> /Core/SPI2_MISO
- U1 pad 18: /BLE/BLE_SPI_CS2 -> /Core/BLE_SPI_CS_2
- U1 pad 22: /BLE/GDO0_1 -> /Core/GDO0_1
- U1 pad 23: /BLE/GDO2_1 -> /Core/GDO2_1
- U1 pad 24: /BLE/GDO0_2 -> /Core/GDO0_2
- U1 pad 25: /BLE/GDO2_2 -> /Core/GDO2_2
- U1 pad 46: /BLE/BLE_SPI_CLK -> /Core/SPI2_SCK
- U10 pad 11: unconnected-(U10-LE-Pad11) -> /Core/LE1
- U10 pad 12: unconnected-(U10-5Q-Pad12) -> Net-(U10-5Q)
- U10 pad 13: unconnected-(U10-5D-Pad13) -> /Core/D5
- U10 pad 14: unconnected-(U10-6D-Pad14) -> /Core/D6
- U10 pad 15: unconnected-(U10-6Q-Pad15) -> Net-(U10-6Q)
- U10 pad 16: unconnected-(U10-7Q-Pad16) -> Net-(U10-7Q)
- U10 pad 17: unconnected-(U10-7D-Pad17) -> /Core/D7
- U10 pad 18: unconnected-(U10-8D-Pad18) -> /Core/D8
- U10 pad 19: unconnected-(U10-8Q-Pad19) -> Net-(U10-8Q)
- U10 pad 20: unconnected-(U10-VCC-Pad20) -> +3.3V
- U10 pad 21: unconnected-(U10-EPAD-Pad21) -> GND
- U11 pad 11: unconnected-(U11-LE-Pad11) -> /Core/LE5
- U11 pad 12: unconnected-(U11-5Q-Pad12) -> Net-(U11-5Q)
- U11 pad 13: unconnected-(U11-5D-Pad13) -> /Core/D5
- U11 pad 14: unconnected-(U11-6D-Pad14) -> /Core/D6
- U11 pad 15: unconnected-(U11-6Q-Pad15) -> Net-(U11-6Q)
- U11 pad 16: unconnected-(U11-7Q-Pad16) -> Net-(U11-7Q)
- U11 pad 17: unconnected-(U11-7D-Pad17) -> /Core/D7
- U11 pad 18: unconnected-(U11-8D-Pad18) -> /Core/D8
- U11 pad 19: unconnected-(U11-8Q-Pad19) -> Net-(U11-8Q)
- U11 pad 20: unconnected-(U11-VCC-Pad20) -> +3.3V
- U11 pad 21: unconnected-(U11-EPAD-Pad21) -> GND
- U12 pad 11: unconnected-(U12-LE-Pad11) -> /Core/LE9
- U12 pad 12: unconnected-(U12-5Q-Pad12) -> Net-(U12-5Q)
- U12 pad 13: unconnected-(U12-5D-Pad13) -> /Core/D5
- U12 pad 14: unconnected-(U12-6D-Pad14) -> /Core/D6
- U12 pad 15: unconnected-(U12-6Q-Pad15) -> Net-(U12-6Q)
- U12 pad 16: unconnected-(U12-7Q-Pad16) -> Net-(U12-7Q)
- U12 pad 17: unconnected-(U12-7D-Pad17) -> /Core/D7
- U12 pad 18: unconnected-(U12-8D-Pad18) -> /Core/D8
- U12 pad 19: unconnected-(U12-8Q-Pad19) -> Net-(U12-8Q)
- U12 pad 20: unconnected-(U12-VCC-Pad20) -> +3.3V
- U12 pad 21: unconnected-(U12-EPAD-Pad21) -> GND
- U13 pad 11: unconnected-(U13-LE-Pad11) -> /Core/LE2
- U13 pad 12: unconnected-(U13-5Q-Pad12) -> Net-(U13-5Q)
- U13 pad 13: unconnected-(U13-5D-Pad13) -> /Core/D5
- U13 pad 14: unconnected-(U13-6D-Pad14) -> /Core/D6
- U13 pad 15: unconnected-(U13-6Q-Pad15) -> Net-(U13-6Q)
- U13 pad 16: unconnected-(U13-7Q-Pad16) -> Net-(U13-7Q)
- U13 pad 17: unconnected-(U13-7D-Pad17) -> /Core/D7
- U13 pad 18: unconnected-(U13-8D-Pad18) -> /Core/D8
- U13 pad 19: unconnected-(U13-8Q-Pad19) -> Net-(U13-8Q)
- U13 pad 20: unconnected-(U13-VCC-Pad20) -> +3.3V
- U13 pad 21: unconnected-(U13-EPAD-Pad21) -> GND
- U14 pad 11: unconnected-(U14-LE-Pad11) -> /Core/LE6
- U14 pad 12: unconnected-(U14-5Q-Pad12) -> Net-(U14-5Q)
- U14 pad 13: unconnected-(U14-5D-Pad13) -> /Core/D5
- U14 pad 14: unconnected-(U14-6D-Pad14) -> /Core/D6
- U14 pad 15: unconnected-(U14-6Q-Pad15) -> Net-(U14-6Q)
- U14 pad 16: unconnected-(U14-7Q-Pad16) -> Net-(U14-7Q)
- U14 pad 17: unconnected-(U14-7D-Pad17) -> /Core/D7
- U14 pad 18: unconnected-(U14-8D-Pad18) -> /Core/D8
- U14 pad 19: unconnected-(U14-8Q-Pad19) -> Net-(U14-8Q)
- U14 pad 20: unconnected-(U14-VCC-Pad20) -> +3.3V
- U14 pad 21: unconnected-(U14-EPAD-Pad21) -> GND
- U15 pad 11: unconnected-(U15-LE-Pad11) -> /Core/LE10
- U15 pad 12: unconnected-(U15-5Q-Pad12) -> Net-(U15-5Q)
- U15 pad 13: unconnected-(U15-5D-Pad13) -> /Core/D5
- U15 pad 14: unconnected-(U15-6D-Pad14) -> /Core/D6
- U15 pad 15: unconnected-(U15-6Q-Pad15) -> Net-(U15-6Q)
- U15 pad 16: unconnected-(U15-7Q-Pad16) -> Net-(U15-7Q)
- U15 pad 17: unconnected-(U15-7D-Pad17) -> /Core/D7
- U15 pad 18: unconnected-(U15-8D-Pad18) -> /Core/D8
- U15 pad 19: unconnected-(U15-8Q-Pad19) -> Net-(U15-8Q)
- U15 pad 20: unconnected-(U15-VCC-Pad20) -> +3.3V
- U15 pad 21: unconnected-(U15-EPAD-Pad21) -> GND
- U16 pad 11: unconnected-(U16-LE-Pad11) -> /Core/LE3
- U16 pad 12: unconnected-(U16-5Q-Pad12) -> Net-(U16-5Q)
- U16 pad 13: unconnected-(U16-5D-Pad13) -> /Core/D5
- U16 pad 14: unconnected-(U16-6D-Pad14) -> /Core/D6
- U16 pad 15: unconnected-(U16-6Q-Pad15) -> Net-(U16-6Q)
- U16 pad 20: unconnected-(U16-VCC-Pad20) -> +3.3V
- U16 pad 21: unconnected-(U16-EPAD-Pad21) -> GND
- U17 pad 11: unconnected-(U17-LE-Pad11) -> /Core/LE7
- U17 pad 12: unconnected-(U17-5Q-Pad12) -> Net-(U17-5Q)
- U17 pad 13: unconnected-(U17-5D-Pad13) -> /Core/D5
- U17 pad 14: unconnected-(U17-6D-Pad14) -> /Core/D6
- U17 pad 15: unconnected-(U17-6Q-Pad15) -> Net-(U17-6Q)
- U17 pad 20: unconnected-(U17-VCC-Pad20) -> +3.3V
- U17 pad 21: unconnected-(U17-EPAD-Pad21) -> GND
- U18 pad 11: unconnected-(U18-LE-Pad11) -> /Core/LE11
- U18 pad 12: unconnected-(U18-5Q-Pad12) -> Net-(U18-5Q)
- U18 pad 13: unconnected-(U18-5D-Pad13) -> /Core/D5
- U18 pad 14: unconnected-(U18-6D-Pad14) -> /Core/D6
- U18 pad 15: unconnected-(U18-6Q-Pad15) -> Net-(U18-6Q)
- U18 pad 16: unconnected-(U18-7Q-Pad16) -> Net-(U18-7Q)
- U18 pad 17: unconnected-(U18-7D-Pad17) -> /Core/D7
- U18 pad 18: unconnected-(U18-8D-Pad18) -> /Core/D8
- U18 pad 19: unconnected-(U18-8Q-Pad19) -> Net-(U18-8Q)
- U18 pad 20: unconnected-(U18-VCC-Pad20) -> +3.3V
- U18 pad 21: unconnected-(U18-EPAD-Pad21) -> GND
- U19 pad 11: unconnected-(U19-LE-Pad11) -> /Core/LE12
- U19 pad 12: unconnected-(U19-5Q-Pad12) -> Net-(U19-5Q)
- U19 pad 13: unconnected-(U19-5D-Pad13) -> /Core/D5
- U19 pad 14: unconnected-(U19-6D-Pad14) -> /Core/D6
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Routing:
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- removed copper zone on In2.Cu, net Net-(D21-K)
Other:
- board text added: "LED ROW 1"
- board text added: "LED ROW 10"
- board text added: "LED ROW 2"
- board text added: "LED ROW 3"
- board text added: "LED ROW 4"
- board text added: "LED ROW 5"
- board text added: "LED ROW 6"
- board text added: "LED ROW 7"
- board text added: "LED ROW 8"
- board text added: "LED ROW 9"
- board text added: "U10"
- board text added: "USB-C Data"
- board text added: "USB-C PD"
- board text removed: "Hij loopd"
